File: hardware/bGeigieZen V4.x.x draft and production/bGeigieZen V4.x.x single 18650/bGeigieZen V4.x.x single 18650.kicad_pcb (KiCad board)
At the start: 2 copper layers, 129.4 x 64.6 mm, 13 parts, among them J1 M5 2x15 pin, J3 GPS, J4 Geiger Safepulse, J5 Extra support header, SW1 SW_SPDT

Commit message: Updated ground fills for NFW and standard boards
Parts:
- moved G*** 1.73 mm to (167.2, 78.0)
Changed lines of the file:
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@@
 	(footprint "bGeigieRaku_M5_1015:18650 map"
 		(layer "B.Cu")
-		(at 165.4921 77.8244 -90)
+		(at 167.2151 78.02 -90)
 		(property "Reference" "G***"
 			(at 0 0 90)

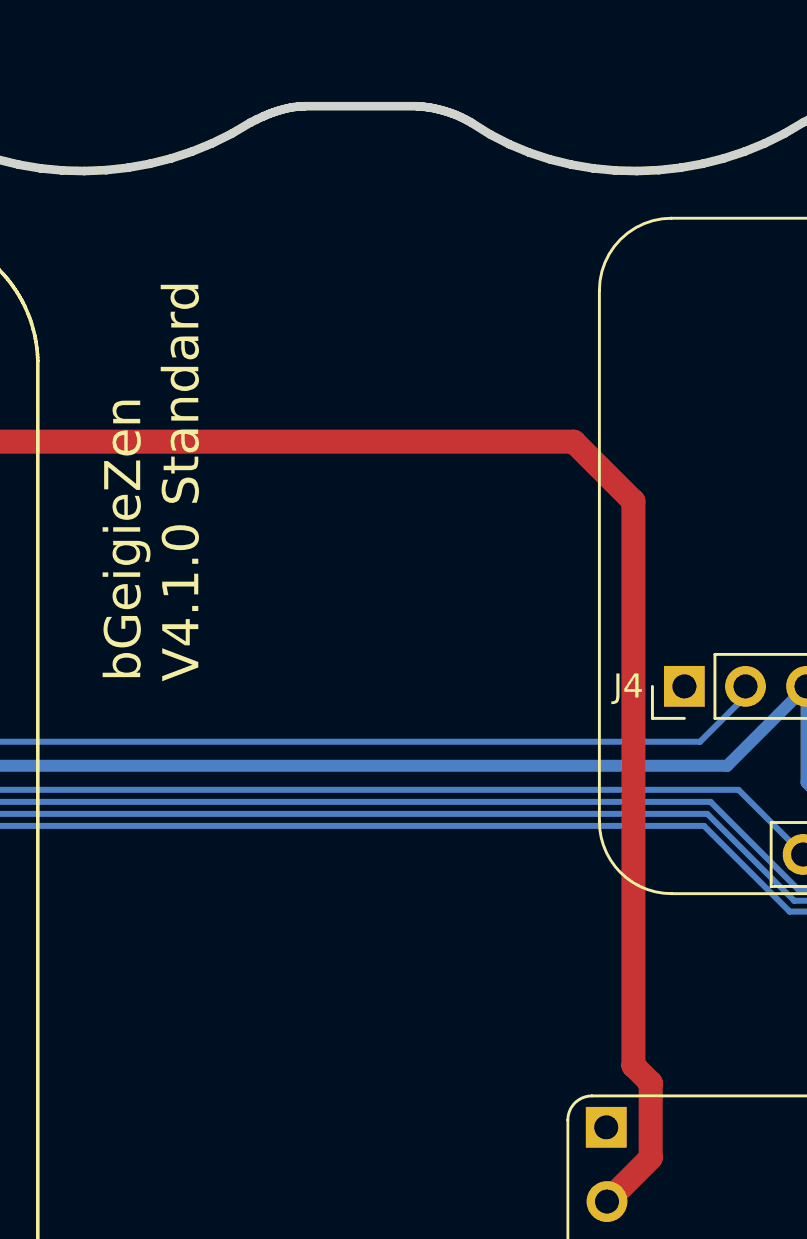
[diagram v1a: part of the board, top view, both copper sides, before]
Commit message: Updated V4.1.1 boards
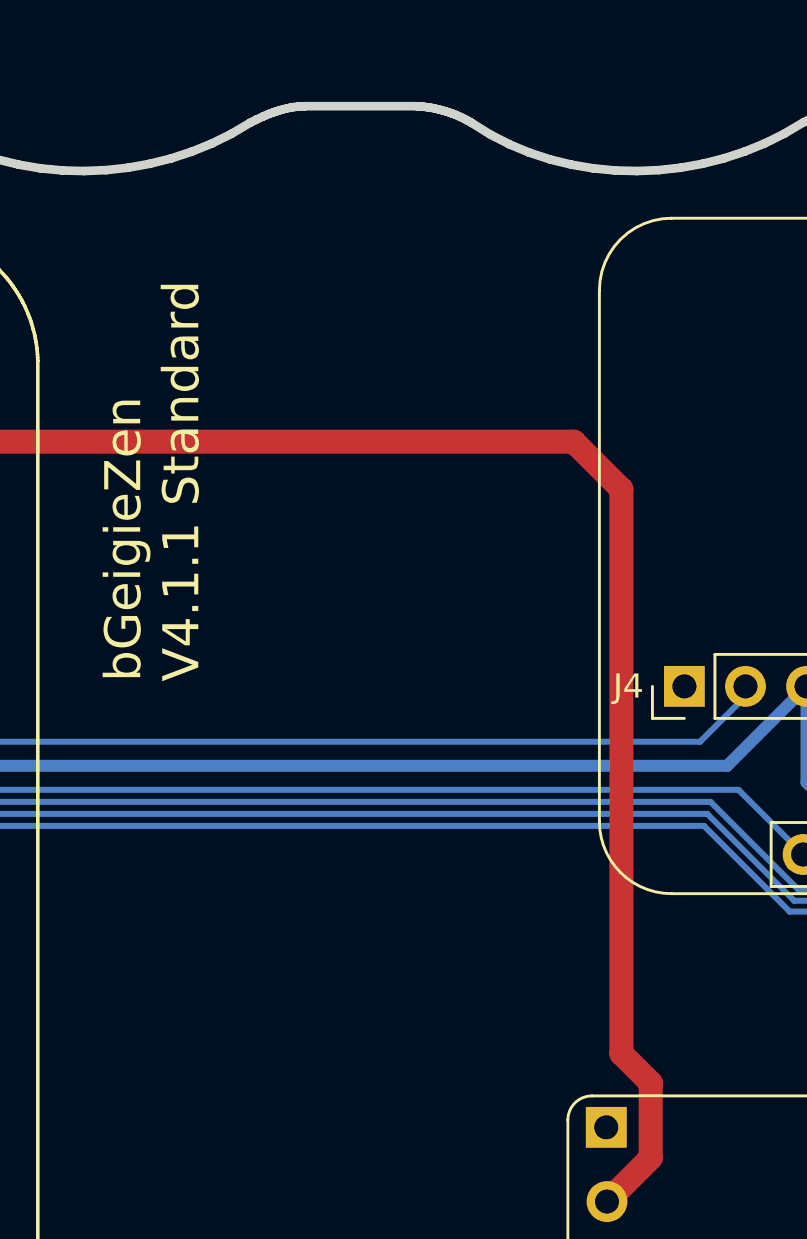
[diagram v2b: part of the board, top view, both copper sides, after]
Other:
- board text added: "bGeigieZen V4.1.1 Standard"
- board text removed: "bGeigieZen V4.1.0 Standard"
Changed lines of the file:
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@@
 	(paper "A4")
 	(title_block
-		(title "bGeigieZen V4.1.0 Standard")
-		(date "2024-12-02")
-		(rev "V4.1.0")
+		(title "bGeigieZen V4.1.1 Standard")
+		(date "2025-03-03")
+		(rev "V4.1.1")
 	)
 	(layers
@@
 		)
 	)
-	(gr_text "bGeigieZen\nV4.1.0 Standard"
+	(gr_text "bGeigieZen\nV4.1.1 Standard"
 		(at 200.8076 108.53 90)
 		(layer "B.SilkS")
@@
 		)
 	)
-	(gr_text "bGeigieZen\nV4.1.0 Standard"
+	(gr_text "bGeigieZen\nV4.1.1 Standard"
 		(at 163.8076 90.53 90)
 		(layer "F.SilkS")
@@
 	)
 	(segment
-		(start 151.2996 80.55)
-		(end 181.3276 80.55)
+		(start 184.5268 110.334884)
+		(end 182.707869 112.153815)
 		(width 1)
 		(layer "F.Cu")
@@
 	)
 	(segment
-		(start 183.8076 83.03)
-		(end 183.8076 106.4972)
+		(start 183.3076 105.9972)
+		(end 184.5268 107.2164)
 		(width 1)
 		(layer "F.Cu")
@@
 	)
 	(segment
-		(start 184.5268 110.334884)
-		(end 182.707869 112.153815)
+		(start 181.3276 80.55)
+		(end 183.3076 82.53)
 		(width 1)
 		(layer "F.Cu")
@@
 	)
 	(segment
-		(start 181.3276 80.55)
-		(end 183.8076 83.03)
+		(start 151.2996 80.55)
+		(end 181.3276 80.55)
 		(width 1)
 		(layer "F.Cu")
@@
 	)
 	(segment
-		(start 183.8076 106.4972)
-		(end 184.5268 107.2164)
+		(start 183.3076 82.53)
+		(end 183.3076 105.9972)
 		(width 1)
 		(layer "F.Cu")
@@
 		(polygon
 			(pts
-				(xy 139.604 70.1776) (xy 154.8652 70.0252) (xy 154.8652 86.3588) (xy 139.7564 86.3588)
+				(xy 135.104 70.1776) (xy 154.8652 70.0252) (xy 154.8652 86.3588) (xy 135.2564 86.3588)
 			)
 		)
@@
 		(polygon
 			(pts
-				(xy 194.8076 70.53) (xy 210.6704 70.53) (xy 210.8076 84.860659) (xy 194.7432 84.7172)
+				(xy 194.8076 70.53) (xy 215.1704 70.53) (xy 215.3076 84.860659) (xy 194.7432 84.7172)
 			)
 		)

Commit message: Board and files updated
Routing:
- net /GIO2 on Core and GIO32 on Core-2: track 83.5 -> 75.2 mm
- net /SCL: track 84.4 -> 76.4 mm
- net /BAT: track 75.7 -> 68.0 mm
- net 3.3V: track 80.6 -> 79.4 mm
- net /SDA: track 86.1 -> 87.0 mm

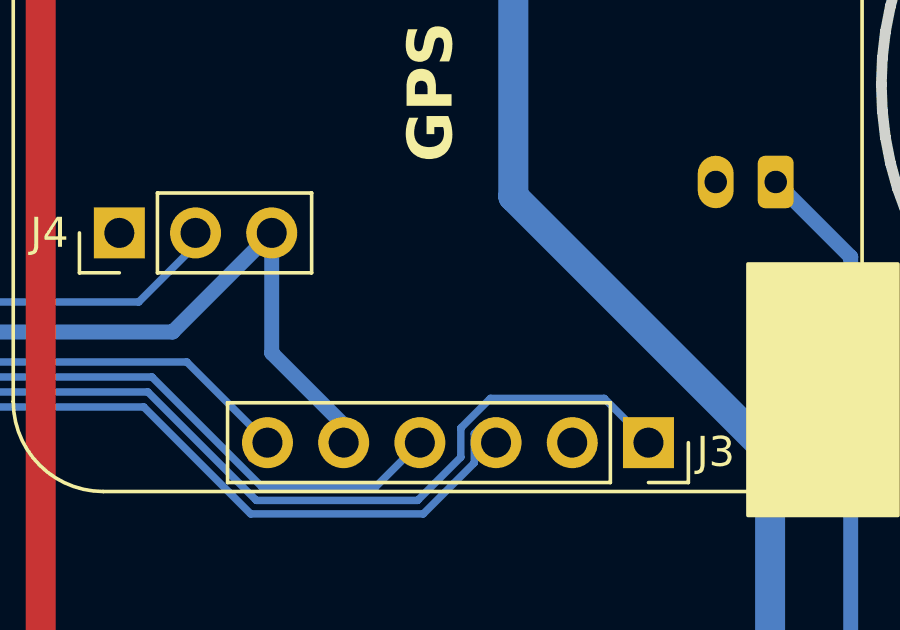
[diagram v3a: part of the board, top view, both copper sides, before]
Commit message: Added lables on boards for GPS wires
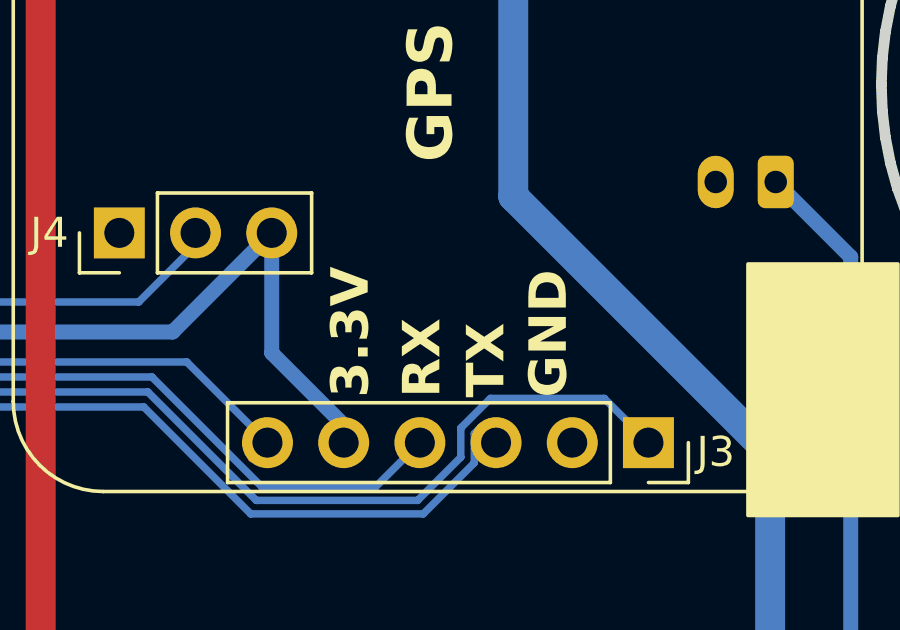
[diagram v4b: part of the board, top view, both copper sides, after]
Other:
- board text added: "3.3V"
- board text added: "GND"
- board text added: "RX"
- board text added: "TX"

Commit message: chore: bump version to v4.1.2 and update default settings
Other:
- board text added: "bGeigieZen V4.1.2 Standard"
- board text removed: "bGeigieZen V4.1.1 Standard"
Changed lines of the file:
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@@
 	(paper "A4")
 	(title_block
-		(title "bGeigieZen V4.1.1 Standard")
-		(date "2025-03-03")
-		(rev "V4.1.1")
+		(title "bGeigieZen V4.1.2 Standard")
+		(date "2025-06-28")
+		(rev "V4.1.2")
 	)
 	(layers
@@
 		)
 	)
-	(gr_text "bGeigieZen\nV4.1.1 Standard"
+	(gr_text "bGeigieZen\nV4.1.2 Standard"
 		(at 163.8076 90.53 90)
 		(layer "F.SilkS")
@@
 		)
 	)
-	(gr_text "bGeigieZen\nV4.1.1 Standard"
+	(gr_text "bGeigieZen\nV4.1.2 Standard"
 		(at 200.8076 108.53 90)
 		(layer "B.SilkS")
